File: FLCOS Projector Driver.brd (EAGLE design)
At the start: 73.9 x 62.1 mm, 79 parts, among them IC1 TLV1117LV33DCYT, IC2 MIC5323-1.8YD5-TR, IC3 MIC5504-2.5YM5-TR, IC4 TVP5150-NTSC_DECODER, IC5 CH340G, IC6 ESP32-WROOM-32UE-N4, IC7 LM3414, IC8 LM3414, IC9 LM3414, J1 MEM2075-00-140-01-A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

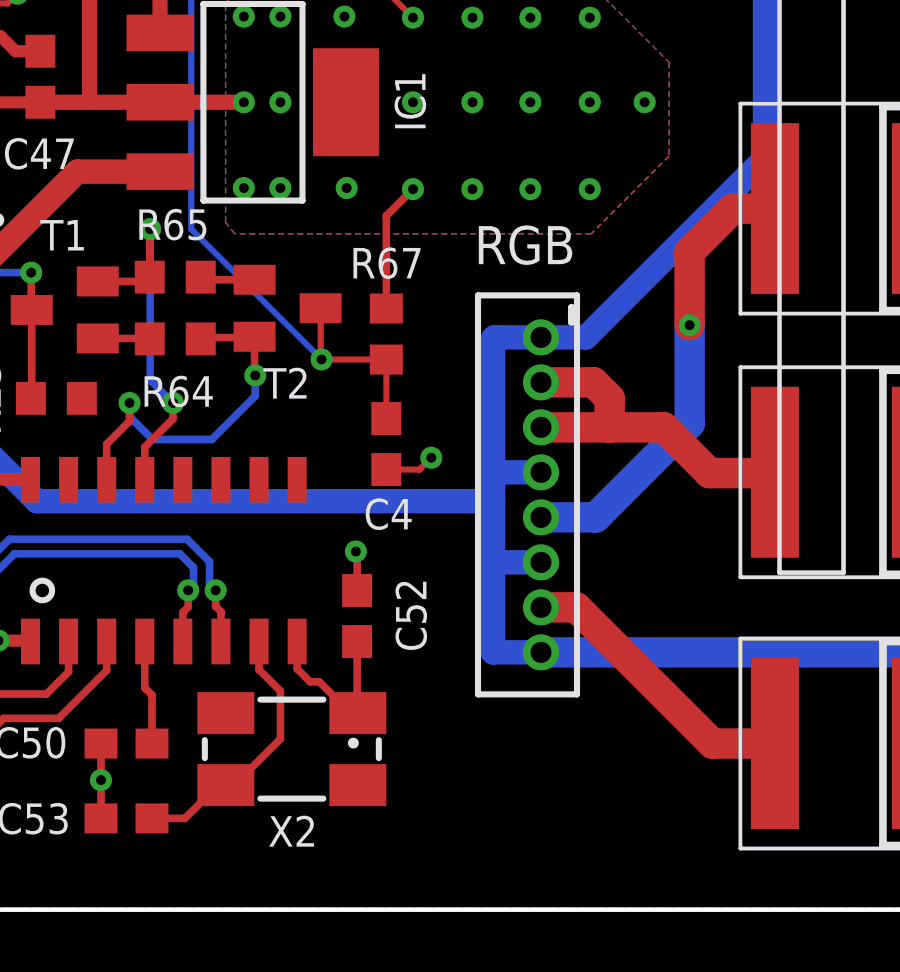
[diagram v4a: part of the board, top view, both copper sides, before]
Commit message: Added JST PH fan header
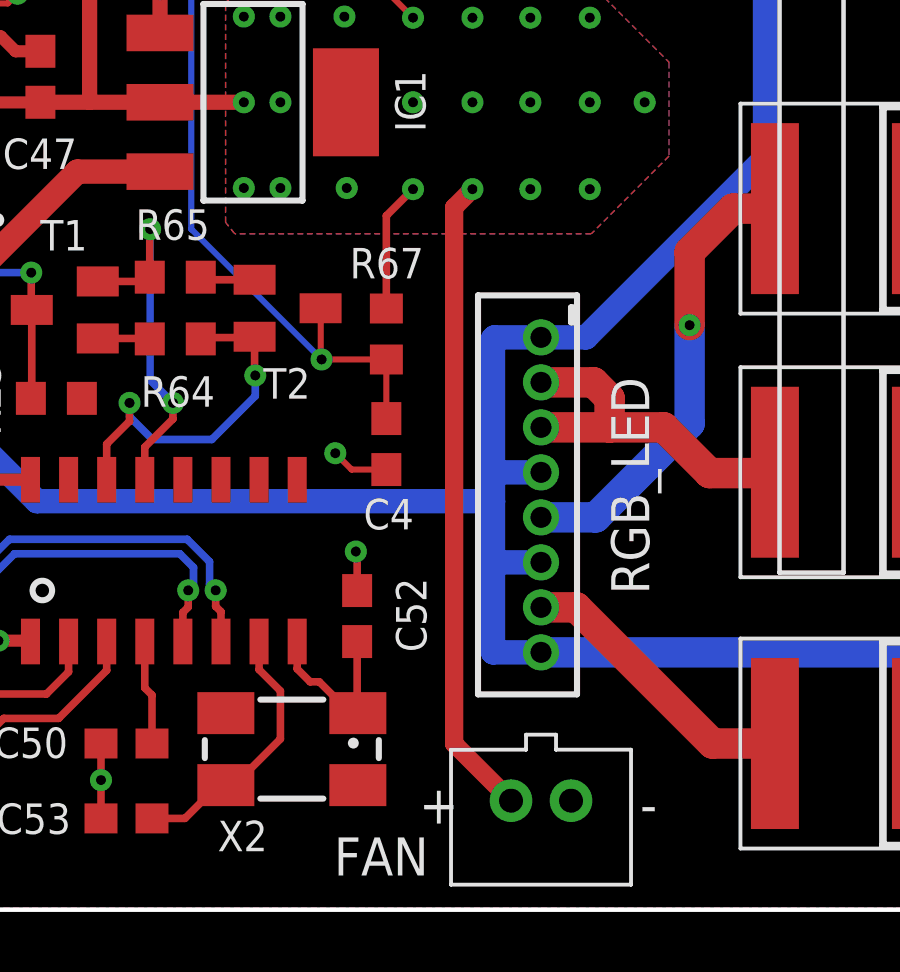
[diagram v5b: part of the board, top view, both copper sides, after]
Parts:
- added FAN: (no value), adafruit:JST-PH-2-THM
- renumbered RGB to RGB_LED
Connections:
- net +3V3: now also FAN.1
- net GND: now also FAN.2
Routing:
- net +3V3: track 115.5 -> 136.9 mm
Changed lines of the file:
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@@
 <attribute name="MF" value="" x="69.5198" y="36.8724" size="1.778" layer="27" rot="R180" display="off"/>
 <attribute name="MPN" value="" x="69.5198" y="36.8724" size="1.778" layer="27" rot="R180" display="off"/>
-<attribute name="NAME" x="31.5722" y="6.9512" size="1.016" layer="25" rot="R180"/>
+<attribute name="NAME" x="29.8958" y="6.7988" size="1.016" layer="25" rot="R180"/>
 <attribute name="OC_FARNELL" value="unknown" x="69.5198" y="36.8724" size="1.778" layer="27" rot="R180" display="off"/>
 <attribute name="OC_NEWARK" value="unknown" x="69.5198" y="36.8724" size="1.778" layer="27" rot="R180" display="off"/>
@@
 <attribute name="VALUE" x="29.2227" y="31.8271" size="0.4064" layer="27" rot="R270"/>
 </element>
-<element name="RGB" library="con-jst" package="ZH-8" value="ZH-8" x="39.0144" y="18.161" smashed="yes" rot="R270">
-<attribute name="NAME" x="36.787" y="25.3506" size="1.27" layer="25"/>
+<element name="RGB_LED" library="con-jst" package="ZH-8" value="ZH-8" x="39.0144" y="18.161" smashed="yes" rot="R270">
+<attribute name="NAME" x="41.3526" y="21.5822" size="1.27" layer="25" rot="R270"/>
 <attribute name="VALUE" x="35.5144" y="23.411" size="1.27" layer="27" rot="R270"/>
 </element>
@@
 <attribute name="NAME" x="21.0058" y="19.6342" size="1.016" layer="25" rot="R90"/>
 <attribute name="VALUE" x="23.495" y="22.7838" size="1.27" layer="27" rot="R180"/>
+</element>
+<element name="FAN" library="adafruit" package="JST-PH-2-THM" value="" x="39.0144" y="7.4676" smashed="yes" rot="R180">
+<attribute name="NAME" x="35.2612" y="6.2432" size="1.27" layer="25" rot="R180"/>
 </element>
 </elements>
@@
 <contactref element="IC9" pad="8"/>
 <contactref element="D3" pad="C"/>
-<contactref element="RGB" pad="1"/>
-<contactref element="RGB" pad="4"/>
-<contactref element="RGB" pad="6"/>
-<contactref element="RGB" pad="8"/>
+<contactref element="RGB_LED" pad="1"/>
+<contactref element="RGB_LED" pad="4"/>
+<contactref element="RGB_LED" pad="6"/>
+<contactref element="RGB_LED" pad="8"/>
 <wire x1="59.0931" y1="16.51" x2="59.0841" y2="16.519" width="0.4064" layer="1"/>
 <wire x1="55.4736" y1="7.4766" x2="55.4826" y2="7.4676" width="0.4064" layer="1"/>
@@
 <wire x1="51.6436" y1="53.1676" x2="51.5112" y2="53.0352" width="0.2032" layer="1"/>
 <contactref element="C4" pad="1"/>
-<wire x1="33.8582" y1="18.5048" x2="34.964" y2="18.5048" width="0.2032" layer="1"/>
-<wire x1="34.964" y1="18.5048" x2="35.3568" y2="18.8976" width="0.2032" layer="1"/>
-<via x="35.3568" y="18.8976" extent="1-16" drill="0.3302"/>
+<via x="32.1564" y="19.05" extent="1-16" drill="0.3302"/>
 <contactref element="R23" pad="1"/>
+<contactref element="FAN" pad="2"/>
+<wire x1="33.8582" y1="18.5048" x2="32.7016" y2="18.5048" width="0.2032" layer="1"/>
+<wire x1="32.7016" y1="18.5048" x2="32.1564" y2="19.05" width="0.2032" layer="1"/>
 </signal>
 <signal name="FLCOS_D7">
@@
 <signal name="GRN_CATHODE">
 <contactref element="L2" pad="2"/>
-<contactref element="RGB" pad="2"/>
-<contactref element="RGB" pad="3"/>
+<contactref element="RGB_LED" pad="2"/>
+<contactref element="RGB_LED" pad="3"/>
 <wire x1="46.7832" y1="18.387" x2="46.8112" y2="18.415" width="1.016" layer="1"/>
 <wire x1="39.0144" y1="19.911" x2="41.3004" y2="19.911" width="1.016" layer="1"/>
@@
 <wire x1="41.8998" y1="60.0354" x2="43.2816" y2="60.0354" width="0.4064" layer="16"/>
 <wire x1="38.862" y1="56.9976" x2="41.8998" y2="60.0354" width="0.4064" layer="16"/>
+<contactref element="FAN" pad="1"/>
+<wire x1="38.0144" y1="7.4676" x2="36.1188" y2="9.3632" width="0.6096" layer="1"/>
+<wire x1="36.1188" y1="27.2424" x2="36.7284" y2="27.852" width="0.6096" layer="1"/>
+<wire x1="36.1188" y1="9.3632" x2="36.1188" y2="27.2424" width="0.6096" layer="1"/>
 </signal>
 <signal name="MOTOR">
@@
 <signal name="RED_CATHODE">
 <contactref element="L1" pad="2"/>
-<contactref element="RGB" pad="5"/>
+<contactref element="RGB_LED" pad="5"/>
 <via x="43.9674" y="23.3172" extent="1-16" drill="0.3302"/>
 <wire x1="46.8112" y1="27.2034" x2="45.4152" y2="27.2034" width="1.016" layer="1"/>
@@
 <signal name="BLU_CATHODE">
 <contactref element="L3" pad="2"/>
-<contactref element="RGB" pad="7"/>
+<contactref element="RGB_LED" pad="7"/>
 <wire x1="44.7294" y1="9.3726" x2="46.8112" y2="9.3726" width="1.016" layer="1"/>
 <wire x1="39.0144" y1="13.911" x2="40.191" y2="13.911" width="1.016" layer="1"/>
